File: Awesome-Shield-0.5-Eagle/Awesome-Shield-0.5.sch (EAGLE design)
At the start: 17 parts, among them J1 ARDUINO_R3_SHIELDUNO_R3_SHIEL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, P1 DNP, P2 DNP, SW1 SPST_TACT-EVQQ2

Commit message: removed 3rd grove port, changed grove port pins
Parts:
- removed J3: (no value), Connector :TWIG-4P-2.0-SMD-FEMALE-REINFORCE'DD'
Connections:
- removed net D4: J1.D4, J3.1
- removed net D7: J1.D7, J3.2
- new net A0: J2.1
- net +5V: no longer J3.3
- net GND: no longer J3.4, J3.SS1, J3.SS2
- net N$2: now also J2.2; no longer J2.1
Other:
- note added: "wifi SD SS"
- note added: "wifi handshake"
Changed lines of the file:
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@@
 <part name="GND7" library="supply1" deviceset="GND" device=""/>
 <part name="P+2" library="supply1" deviceset="+5V" device=""/>
-<part name="P+3" library="supply1" deviceset="+5V" device=""/>
-<part name="GND8" library="supply1" deviceset="GND" device=""/>
 <part name="J5" library="Connector " deviceset="TWIG-4P-2.0-SMD-FEMALE-REINFORCE" device="'DD'"/>
 <part name="GND9" library="supply1" deviceset="GND" device=""/>
 <part name="J2" library="Connector " deviceset="TWIG-4P-2.0-SMD-FEMALE-REINFORCE" device="'DD'"/>
 <part name="GND10" library="supply1" deviceset="GND" device=""/>
-<part name="J3" library="Connector " deviceset="TWIG-4P-2.0-SMD-FEMALE-REINFORCE" device="'DD'"/>
-<part name="GND11" library="supply1" deviceset="GND" device=""/>
 <part name="P1" library="Discrete" deviceset="PAD-JUMPER-2P" device="" value="DNP"/>
 <part name="P2" library="Discrete" deviceset="PAD-JUMPER-2P" device="" value="DNP"/>
@@
 <text x="208.28" y="121.285" size="1.778" layer="91">SPI</text>
 <text x="208.28" y="113.665" size="1.778" layer="91">SPI</text>
+<text x="208.28" y="128.905" size="1.778" layer="91">wifi handshake</text>
+<text x="208.28" y="136.525" size="1.778" layer="91">wifi SD SS</text>
 </plain>
 <instances>
@@
 <instance part="GND7" gate="1" x="269.24" y="73.66"/>
 <instance part="P+2" gate="1" x="269.24" y="91.44"/>
-<instance part="P+3" gate="1" x="309.88" y="91.44"/>
-<instance part="GND8" gate="1" x="309.88" y="73.66"/>
 <instance part="J5" gate="G$1" x="180.34" y="57.15"/>
 <instance part="GND9" gate="1" x="180.34" y="43.18"/>
 <instance part="J2" gate="G$1" x="287.02" y="85.09"/>
 <instance part="GND10" gate="1" x="287.02" y="71.12"/>
-<instance part="J3" gate="G$1" x="327.66" y="85.09"/>
-<instance part="GND11" gate="1" x="327.66" y="71.12"/>
 <instance part="P1" gate="G$1" x="201.93" y="91.44" rot="R270"/>
 <instance part="P2" gate="G$1" x="201.93" y="73.66" rot="R90"/>
@@
 </segment>
 <segment>
-<pinref part="GND8" gate="1" pin="GND"/>
-<wire x1="309.88" y1="76.2" x2="309.88" y2="78.74" width="0.1524" layer="91"/>
-<wire x1="309.88" y1="78.74" x2="312.42" y2="81.28" width="0.1524" layer="91"/>
-<wire x1="312.42" y1="81.28" x2="322.58" y2="81.28" width="0.1524" layer="91"/>
-<pinref part="J3" gate="G$1" pin="4"/>
-</segment>
-<segment>
 <wire x1="281.94" y1="81.28" x2="271.78" y2="81.28" width="0.1524" layer="91"/>
 <wire x1="271.78" y1="81.28" x2="269.24" y2="78.74" width="0.1524" layer="91"/>
@@
 <wire x1="287.02" y1="76.2" x2="287.02" y2="73.66" width="0.1524" layer="91"/>
 <junction x="287.02" y="76.2"/>
-</segment>
-<segment>
-<pinref part="J3" gate="G$1" pin="SS1"/>
-<wire x1="327.66" y1="92.71" x2="330.2" y2="95.25" width="0.1524" layer="91"/>
-<wire x1="330.2" y1="95.25" x2="332.74" y2="95.25" width="0.1524" layer="91"/>
-<wire x1="332.74" y1="95.25" x2="334.01" y2="93.98" width="0.1524" layer="91"/>
-<wire x1="334.01" y1="93.98" x2="334.01" y2="77.47" width="0.1524" layer="91"/>
-<wire x1="334.01" y1="77.47" x2="332.74" y2="76.2" width="0.1524" layer="91"/>
-<wire x1="332.74" y1="76.2" x2="327.66" y2="76.2" width="0.1524" layer="91"/>
-<pinref part="J3" gate="G$1" pin="SS2"/>
-<wire x1="327.66" y1="76.2" x2="327.66" y2="77.47" width="0.1524" layer="91"/>
-<pinref part="GND11" gate="1" pin="GND"/>
-<wire x1="327.66" y1="76.2" x2="327.66" y2="73.66" width="0.1524" layer="91"/>
-<junction x="327.66" y="76.2"/>
 </segment>
 <segment>
@@
 </segment>
 <segment>
-<wire x1="322.58" y1="83.82" x2="312.42" y2="83.82" width="0.1524" layer="91"/>
-<wire x1="312.42" y1="83.82" x2="309.88" y2="86.36" width="0.1524" layer="91"/>
-<pinref part="P+3" gate="1" pin="+5V"/>
-<wire x1="309.88" y1="86.36" x2="309.88" y2="88.9" width="0.1524" layer="91"/>
-<pinref part="J3" gate="G$1" pin="3"/>
-</segment>
-<segment>
 <wire x1="281.94" y1="83.82" x2="271.78" y2="83.82" width="0.1524" layer="91"/>
 <wire x1="271.78" y1="83.82" x2="269.24" y2="86.36" width="0.1524" layer="91"/>
@@
 <net name="N$2" class="0">
 <segment>
-<wire x1="276.86" y1="91.44" x2="276.86" y2="101.6" width="0.1524" layer="91"/>
-<wire x1="281.94" y1="88.9" x2="279.4" y2="88.9" width="0.1524" layer="91"/>
-<wire x1="279.4" y1="88.9" x2="276.86" y2="91.44" width="0.1524" layer="91"/>
-<wire x1="276.86" y1="101.6" x2="254" y2="124.46" width="0.1524" layer="91"/>
 <pinref part="J1" gate="G$1" pin="*D9"/>
+<wire x1="274.32" y1="104.14" x2="254" y2="124.46" width="0.1524" layer="91"/>
 <wire x1="254" y1="124.46" x2="208.28" y2="124.46" width="0.1524" layer="91"/>
-<pinref part="J2" gate="G$1" pin="1"/>
-</segment>
-</net>
-<net name="D4" class="0">
-<segment>
-<wire x1="322.58" y1="88.9" x2="320.04" y2="88.9" width="0.1524" layer="91"/>
-<wire x1="320.04" y1="88.9" x2="317.5" y2="91.44" width="0.1524" layer="91"/>
-<wire x1="317.5" y1="91.44" x2="317.5" y2="101.6" width="0.1524" layer="91"/>
-<wire x1="317.5" y1="101.6" x2="312.42" y2="106.68" width="0.1524" layer="91"/>
-<wire x1="312.42" y1="106.68" x2="307.34" y2="106.68" width="0.1524" layer="91"/>
-<label x="307.34" y="106.68" size="1.778" layer="95"/>
-<pinref part="J3" gate="G$1" pin="1"/>
-</segment>
-<segment>
-<pinref part="J1" gate="G$1" pin="D4"/>
-<wire x1="208.28" y1="137.16" x2="213.36" y2="137.16" width="0.1524" layer="91"/>
-</segment>
-</net>
-<net name="D7" class="0">
-<segment>
-<wire x1="322.58" y1="86.36" x2="320.04" y2="86.36" width="0.1524" layer="91"/>
-<wire x1="320.04" y1="86.36" x2="314.96" y2="91.44" width="0.1524" layer="91"/>
-<wire x1="314.96" y1="91.44" x2="314.96" y2="101.6" width="0.1524" layer="91"/>
-<wire x1="314.96" y1="101.6" x2="312.42" y2="104.14" width="0.1524" layer="91"/>
-<wire x1="312.42" y1="104.14" x2="307.34" y2="104.14" width="0.1524" layer="91"/>
-<label x="307.34" y="104.14" size="1.778" layer="95"/>
-<pinref part="J3" gate="G$1" pin="2"/>
-</segment>
-<segment>
-<pinref part="J1" gate="G$1" pin="D7"/>
-<wire x1="208.28" y1="129.54" x2="213.36" y2="129.54" width="0.1524" layer="91"/>
+<pinref part="J2" gate="G$1" pin="2"/>
+<wire x1="281.94" y1="86.36" x2="276.86" y2="86.36" width="0.1524" layer="91"/>
+<wire x1="276.86" y1="86.36" x2="274.32" y2="88.9" width="0.1524" layer="91"/>
+<wire x1="274.32" y1="88.9" x2="274.32" y2="104.14" width="0.1524" layer="91"/>
 </segment>
 </net>
@@
 </segment>
 </net>
+<net name="A0" class="0">
+<segment>
+<pinref part="J2" gate="G$1" pin="1"/>
+<wire x1="281.94" y1="88.9" x2="279.4" y2="88.9" width="0.1524" layer="91"/>
+<label x="279.4" y="88.9" size="1.778" layer="95"/>
+</segment>
+</net>

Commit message: added dummy buzzer
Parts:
- added SG1: BUZZERSMD2, SparkFun-Electromechanical:BUZZERSMD2
- added SG3: BUZZERSMD, SparkFun-Electromechanical:BUZZERSMD
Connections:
- net A0: now also J1.A0
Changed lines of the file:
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@@
 <setting verticaltext="up"/>
 </settings>
-<grid distance="0.1" unitdist="inch" unit="inch" style="lines" multiple="1" display="yes" altdistance="0.025" altunitdist="inch" altunit="inch"/>
+<grid distance="0.1" unitdist="inch" unit="inch" style="lines" multiple="1" display="no" altdistance="0.01" altunitdist="inch" altunit="inch"/>
 <layers>
 <layer number="1" name="Top" color="4" fill="1" visible="no" active="no"/>
@@
 <part name="S1" library="smd-special" deviceset="SWS001" device=""/>
 <part name="GND12" library="supply1" deviceset="GND" device=""/>
+<part name="SG1" library="SparkFun-Electromechanical" deviceset="BUZZER" device="SMD2"/>
+<part name="SG3" library="SparkFun-Electromechanical" deviceset="BUZZER" device="SMD"/>
 </parts>
 <sheets>
@@
 <instance part="S1" gate="G$1" x="337.82" y="157.48"/>
 <instance part="GND12" gate="1" x="337.82" y="139.7"/>
+<instance part="SG1" gate="G$1" x="124.46" y="160.02"/>
+<instance part="SG3" gate="G$1" x="139.7" y="144.78"/>
 </instances>
 <busses>
@@
 <label x="279.4" y="88.9" size="1.778" layer="95"/>
 </segment>
-</net>
+<segment>
+<pinref part="J1" gate="G$1" pin="A0"/>
+<wire x1="182.88" y1="149.86" x2="177.8" y2="149.86" width="0.1524" layer="91"/>
+</segment>
+</net>

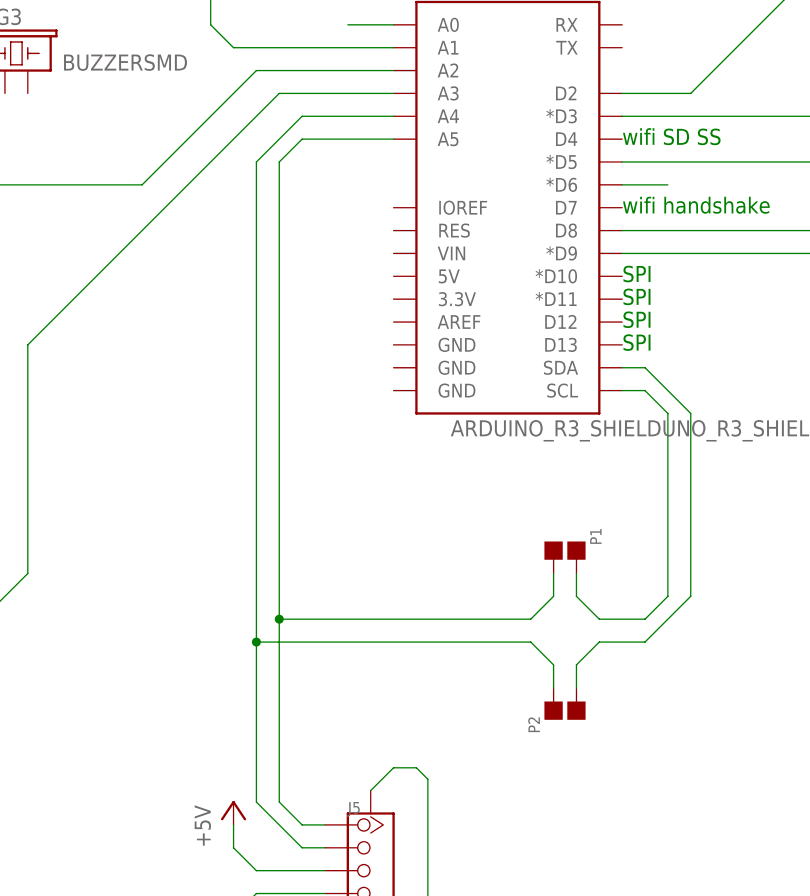
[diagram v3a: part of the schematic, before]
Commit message: adjusted tact switch and buzzer landing areas, moved jumpers to A4 and A5 traces
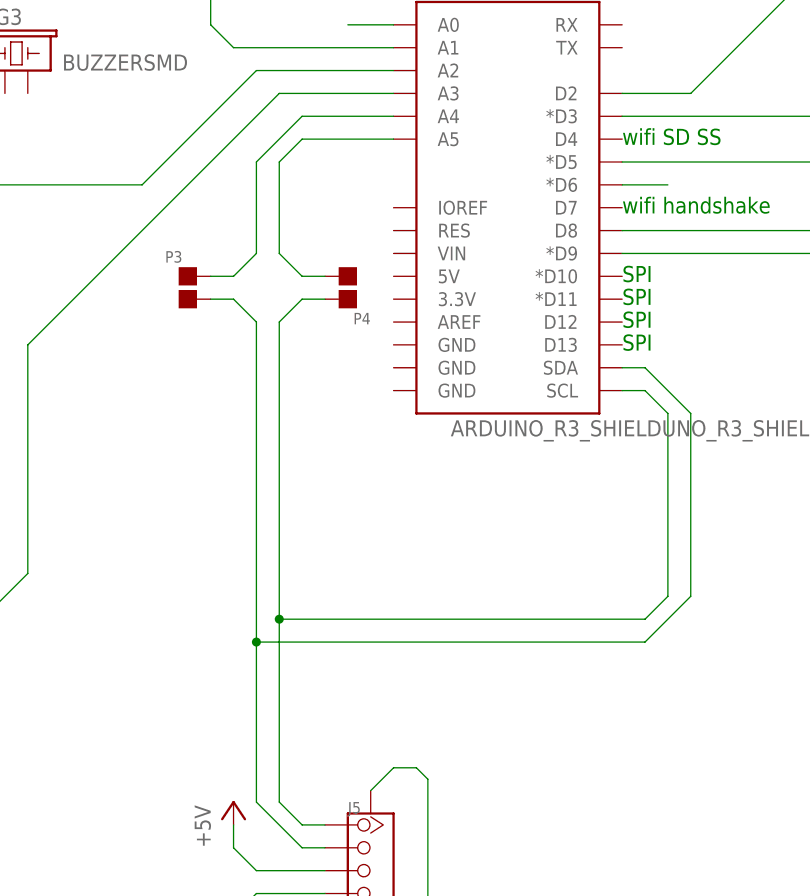
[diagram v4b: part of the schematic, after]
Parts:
- removed P1, P2: DNP, Discrete:PAD-JUMPER-2P
- added P3, P4: DNP, Discrete:PAD-JUMPER-2P
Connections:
- net A4: now also P3.2; no longer J5.2, P2.2
- net A5: now also P4.1; no longer J5.1, P1.1
- net SCL: now also J5.1, P4.2; no longer P1.2
- net SDA: now also J5.2, P3.1; no longer P2.1
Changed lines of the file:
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@@
 <part name="J2" library="Connector " deviceset="TWIG-4P-2.0-SMD-FEMALE-REINFORCE" device="'DD'"/>
 <part name="GND10" library="supply1" deviceset="GND" device=""/>
-<part name="P1" library="Discrete" deviceset="PAD-JUMPER-2P" device="" value="DNP"/>
-<part name="P2" library="Discrete" deviceset="PAD-JUMPER-2P" device="" value="DNP"/>
 <part name="S1" library="smd-special" deviceset="SWS001" device=""/>
 <part name="GND12" library="supply1" deviceset="GND" device=""/>
 <part name="SG1" library="SparkFun-Electromechanical" deviceset="BUZZER" device="SMD2"/>
 <part name="SG3" library="SparkFun-Electromechanical" deviceset="BUZZER" device="SMD"/>
+<part name="P3" library="Discrete" deviceset="PAD-JUMPER-2P" device="" value="DNP"/>
+<part name="P4" library="Discrete" deviceset="PAD-JUMPER-2P" device="" value="DNP"/>
 </parts>
 <sheets>
@@
 <instance part="J2" gate="G$1" x="287.02" y="85.09"/>
 <instance part="GND10" gate="1" x="287.02" y="71.12"/>
-<instance part="P1" gate="G$1" x="201.93" y="91.44" rot="R270"/>
-<instance part="P2" gate="G$1" x="201.93" y="73.66" rot="R90"/>
 <instance part="S1" gate="G$1" x="337.82" y="157.48"/>
 <instance part="GND12" gate="1" x="337.82" y="139.7"/>
 <instance part="SG1" gate="G$1" x="124.46" y="160.02"/>
 <instance part="SG3" gate="G$1" x="139.7" y="144.78"/>
+<instance part="P3" gate="G$1" x="160.02" y="120.65"/>
+<instance part="P4" gate="G$1" x="177.8" y="120.65" rot="R180"/>
 </instances>
 <busses>
@@
 </segment>
 </net>
-<net name="A4" class="0">
-<segment>
-<wire x1="167.64" y1="134.62" x2="172.72" y2="139.7" width="0.1524" layer="91"/>
-<pinref part="J1" gate="G$1" pin="A4"/>
-<wire x1="172.72" y1="139.7" x2="182.88" y2="139.7" width="0.1524" layer="91"/>
-<wire x1="167.64" y1="134.62" x2="167.64" y2="81.28" width="0.1524" layer="91"/>
-<pinref part="J5" gate="G$1" pin="2"/>
-<wire x1="172.72" y1="58.42" x2="167.64" y2="63.5" width="0.1524" layer="91"/>
-<wire x1="172.72" y1="58.42" x2="175.26" y2="58.42" width="0.1524" layer="91"/>
-<wire x1="167.64" y1="81.28" x2="167.64" y2="63.5" width="0.1524" layer="91"/>
-<junction x="167.64" y="81.28"/>
-<pinref part="P2" gate="G$1" pin="2"/>
-<wire x1="200.66" y1="76.2" x2="200.66" y2="78.74" width="0.1524" layer="91"/>
-<wire x1="200.66" y1="78.74" x2="198.12" y2="81.28" width="0.1524" layer="91"/>
-<wire x1="198.12" y1="81.28" x2="167.64" y2="81.28" width="0.1524" layer="91"/>
-</segment>
-</net>
 <net name="D6" class="0">
 <segment>
@@
 <wire x1="276.86" y1="86.36" x2="274.32" y2="88.9" width="0.1524" layer="91"/>
 <wire x1="274.32" y1="88.9" x2="274.32" y2="104.14" width="0.1524" layer="91"/>
-</segment>
-</net>
-<net name="A5" class="0">
-<segment>
-<pinref part="J5" gate="G$1" pin="1"/>
-<wire x1="170.18" y1="63.5" x2="172.72" y2="60.96" width="0.1524" layer="91"/>
-<wire x1="172.72" y1="60.96" x2="175.26" y2="60.96" width="0.1524" layer="91"/>
-<wire x1="170.18" y1="63.5" x2="170.18" y2="83.82" width="0.1524" layer="91"/>
-<junction x="170.18" y="83.82"/>
-<wire x1="200.66" y1="88.9" x2="200.66" y2="86.36" width="0.1524" layer="91"/>
-<wire x1="200.66" y1="86.36" x2="198.12" y2="83.82" width="0.1524" layer="91"/>
-<wire x1="198.12" y1="83.82" x2="170.18" y2="83.82" width="0.1524" layer="91"/>
-<pinref part="P1" gate="G$1" pin="1"/>
-<pinref part="J1" gate="G$1" pin="A5"/>
-<wire x1="182.88" y1="137.16" x2="172.72" y2="137.16" width="0.1524" layer="91"/>
-<wire x1="172.72" y1="137.16" x2="170.18" y2="134.62" width="0.1524" layer="91"/>
-<wire x1="170.18" y1="83.82" x2="170.18" y2="134.62" width="0.1524" layer="91"/>
 </segment>
 </net>
@@
 </segment>
 </net>
+<net name="A0" class="0">
+<segment>
+<pinref part="J2" gate="G$1" pin="1"/>
+<wire x1="281.94" y1="88.9" x2="279.4" y2="88.9" width="0.1524" layer="91"/>
+<label x="279.4" y="88.9" size="1.778" layer="95"/>
+</segment>
+<segment>
+<pinref part="J1" gate="G$1" pin="A0"/>
+<wire x1="182.88" y1="149.86" x2="177.8" y2="149.86" width="0.1524" layer="91"/>
+</segment>
+</net>
+<net name="A4" class="0">
+<segment>
+<wire x1="165.1" y1="121.92" x2="162.56" y2="121.92" width="0.1524" layer="91"/>
+<pinref part="P3" gate="G$1" pin="2"/>
+<wire x1="167.64" y1="124.46" x2="165.1" y2="121.92" width="0.1524" layer="91"/>
+<pinref part="J1" gate="G$1" pin="A4"/>
+<wire x1="172.72" y1="139.7" x2="182.88" y2="139.7" width="0.1524" layer="91"/>
+<wire x1="167.64" y1="134.62" x2="172.72" y2="139.7" width="0.1524" layer="91"/>
+<wire x1="167.64" y1="124.46" x2="167.64" y2="134.62" width="0.1524" layer="91"/>
+</segment>
+</net>
+<net name="A5" class="0">
+<segment>
+<wire x1="170.18" y1="124.46" x2="172.72" y2="121.92" width="0.1524" layer="91"/>
+<pinref part="P4" gate="G$1" pin="1"/>
+<wire x1="172.72" y1="121.92" x2="175.26" y2="121.92" width="0.1524" layer="91"/>
+<pinref part="J1" gate="G$1" pin="A5"/>
+<wire x1="182.88" y1="137.16" x2="172.72" y2="137.16" width="0.1524" layer="91"/>
+<wire x1="172.72" y1="137.16" x2="170.18" y2="134.62" width="0.1524" layer="91"/>
+<wire x1="170.18" y1="134.62" x2="170.18" y2="124.46" width="0.1524" layer="91"/>
+</segment>
+</net>
 <net name="SCL" class="0">
 <segment>
+<pinref part="P4" gate="G$1" pin="2"/>
+<wire x1="175.26" y1="119.38" x2="172.72" y2="119.38" width="0.1524" layer="91"/>
+<wire x1="172.72" y1="119.38" x2="170.18" y2="116.84" width="0.1524" layer="91"/>
+<wire x1="170.18" y1="116.84" x2="170.18" y2="83.82" width="0.1524" layer="91"/>
+<pinref part="J5" gate="G$1" pin="1"/>
+<wire x1="170.18" y1="63.5" x2="172.72" y2="60.96" width="0.1524" layer="91"/>
+<wire x1="172.72" y1="60.96" x2="175.26" y2="60.96" width="0.1524" layer="91"/>
+<wire x1="170.18" y1="63.5" x2="170.18" y2="83.82" width="0.1524" layer="91"/>
+<wire x1="210.82" y1="83.82" x2="170.18" y2="83.82" width="0.1524" layer="91"/>
+<junction x="170.18" y="83.82"/>
 <pinref part="J1" gate="G$1" pin="SCL"/>
 <wire x1="210.82" y1="109.22" x2="208.28" y2="109.22" width="0.1524" layer="91"/>
@@
 <wire x1="213.36" y1="106.68" x2="213.36" y2="86.36" width="0.1524" layer="91"/>
 <wire x1="213.36" y1="86.36" x2="210.82" y2="83.82" width="0.1524" layer="91"/>
-<wire x1="210.82" y1="83.82" x2="205.74" y2="83.82" width="0.1524" layer="91"/>
-<wire x1="205.74" y1="83.82" x2="203.2" y2="86.36" width="0.1524" layer="91"/>
-<wire x1="203.2" y1="86.36" x2="203.2" y2="88.9" width="0.1524" layer="91"/>
-<pinref part="P1" gate="G$1" pin="2"/>
 </segment>
 </net>
 <net name="SDA" class="0">
 <segment>
+<wire x1="162.56" y1="119.38" x2="165.1" y2="119.38" width="0.1524" layer="91"/>
+<wire x1="165.1" y1="119.38" x2="167.64" y2="116.84" width="0.1524" layer="91"/>
+<wire x1="167.64" y1="116.84" x2="167.64" y2="81.28" width="0.1524" layer="91"/>
+<pinref part="P3" gate="G$1" pin="1"/>
+<pinref part="J5" gate="G$1" pin="2"/>
+<wire x1="172.72" y1="58.42" x2="167.64" y2="63.5" width="0.1524" layer="91"/>
+<wire x1="172.72" y1="58.42" x2="175.26" y2="58.42" width="0.1524" layer="91"/>
+<wire x1="167.64" y1="81.28" x2="167.64" y2="63.5" width="0.1524" layer="91"/>
+<wire x1="210.82" y1="81.28" x2="167.64" y2="81.28" width="0.1524" layer="91"/>
+<junction x="167.64" y="81.28"/>
 <pinref part="J1" gate="G$1" pin="SDA"/>
 <wire x1="208.28" y1="111.76" x2="210.82" y2="111.76" width="0.1524" layer="91"/>
@@
 <wire x1="215.9" y1="106.68" x2="215.9" y2="86.36" width="0.1524" layer="91"/>
 <wire x1="215.9" y1="86.36" x2="210.82" y2="81.28" width="0.1524" layer="91"/>
-<wire x1="210.82" y1="81.28" x2="205.74" y2="81.28" width="0.1524" layer="91"/>
-<wire x1="205.74" y1="81.28" x2="203.2" y2="78.74" width="0.1524" layer="91"/>
-<pinref part="P2" gate="G$1" pin="1"/>
-<wire x1="203.2" y1="78.74" x2="203.2" y2="76.2" width="0.1524" layer="91"/>
-</segment>
-</net>
-<net name="A0" class="0">
-<segment>
-<pinref part="J2" gate="G$1" pin="1"/>
-<wire x1="281.94" y1="88.9" x2="279.4" y2="88.9" width="0.1524" layer="91"/>
-<label x="279.4" y="88.9" size="1.778" layer="95"/>
-</segment>
-<segment>
-<pinref part="J1" gate="G$1" pin="A0"/>
-<wire x1="182.88" y1="149.86" x2="177.8" y2="149.86" width="0.1524" layer="91"/>
-</segment>
-</net>
+</segment>
+</net>
